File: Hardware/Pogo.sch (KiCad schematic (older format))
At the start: 3 parts

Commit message: Adjusted beginning schematics. Not much there yet
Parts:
- removed P?: CONN_6, symbol CONN_6
- added P? (x2): CONN_5X2, symbol CONN_5X2
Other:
- moved on the sheet: P?
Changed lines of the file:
@@
-EESchema Schematic File Version 2  date 5/6/2012 4:36:42 PM
+EESchema Schematic File Version 2  date 5/11/2012 5:03:51 PM
 LIBS:power
 LIBS:device
@@
 LIBS:contrib
 LIBS:valves
-EELAYER 43  0
+LIBS:Pogo-cache
+EELAYER 25  0
 EELAYER END
 $Descr A4 11700 8267
@@
 Sheet 1 1
 Title "Pogo"
-Date "6 may 2012"
+Date "12 may 2012"
 Rev "1.0"
 Comp "Projects and Stuff LLC"
@@
 $EndDescr
 $Comp
-L CONN_6 P?
-U 1 1 4FA6D806
-P 5350 3150
-F 0 "P?" V 5300 3150 60  0000 C CNN
-F 1 "CONN_6" V 5400 3150 60  0000 C CNN
-	1    5350 3150
+L CONN_5X2 P?
+U 1 1 4FADA8DA
+P 5350 3250
+F 0 "P?" H 5350 3550 60  0000 C CNN
+F 1 "CONN_5X2" V 5350 3250 50  0000 C CNN
+	1    5350 3250
+	1    0    0    -1
+$EndComp
+$Comp
+L CONN_5X2 P?
+U 1 1 4FADA8D4
+P 2650 3250
+F 0 "P?" H 2650 3550 60  0000 C CNN
+F 1 "CONN_5X2" V 2650 3250 50  0000 C CNN
+	1    2650 3250
 	1    0    0    -1
 $EndComp
@@
 L CONN_3X2 P?
 U 1 1 4FA6D7FB
-P 5350 2300
-F 0 "P?" H 5350 2550 50  0000 C CNN
-F 1 "CONN_3X2" V 5350 2350 40  0000 C CNN
-	1    5350 2300
+P 5350 2350
+F 0 "P?" H 5350 2600 50  0000 C CNN
+F 1 "CONN_3X2" V 5350 2400 40  0000 C CNN
+	1    5350 2350
 	1    0    0    -1
 $EndComp

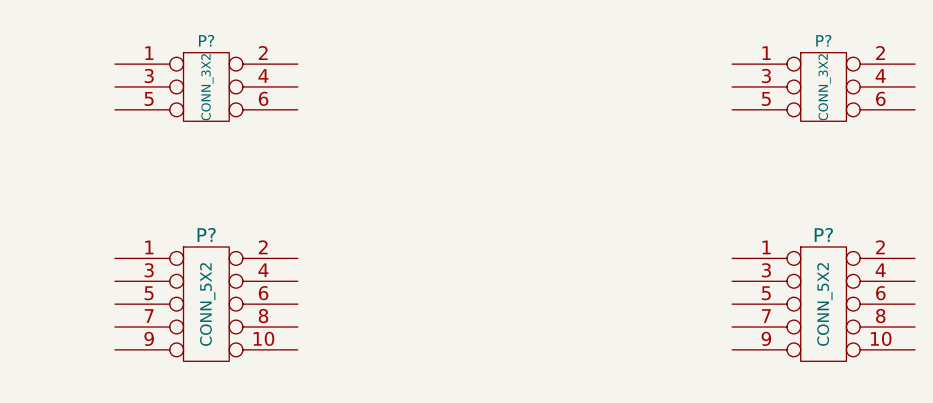
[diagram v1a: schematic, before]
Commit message: Converted BOM and updated Schematics and Board
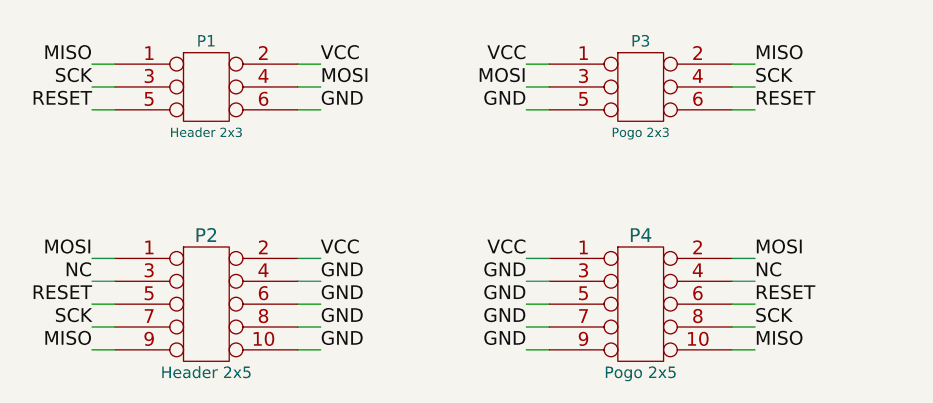
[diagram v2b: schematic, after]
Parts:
- removed P?: CONN_3X2, symbol CONN_3X2
- removed P?: CONN_5X2, symbol CONN_5X2
- added P3: Pogo 2x3, symbol CONN_3X2
- added P4: Pogo 2x5, symbol CONN_5X2
- P1: renamed from P?; value CONN_3X2 -> Header 2x3
- P2: renamed from P?; value CONN_5X2 -> Header 2x5
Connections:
- net MISO: now reaches P1.1
- net MISO: now also P2.9, P3.2, P4.10
- net VCC: now reaches P1.2
- net VCC: now also P2.2, P3.1, P4.1
- net SCK: now reaches P1.3
- net SCK: now also P2.7, P3.4, P4.8
- net MOSI: now reaches P1.4
- net MOSI: now also P2.1, P3.3, P4.2
- net RESET: now reaches P1.5
- net RESET: now also P2.5, P3.6, P4.6
- net GND: now reaches P1.6
- net GND: now also P2.10, P2.4, P2.6, P2.8, P3.5, P4.3, P4.5, P4.7, P4.9
- net NC: now reaches P2.3
- net NC: now also P4.4
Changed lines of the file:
@@
-EESchema Schematic File Version 2  date 5/11/2012 5:03:51 PM
+EESchema Schematic File Version 2  date 7/3/2012 7:28:53 PM
 LIBS:power
 LIBS:device
@@
 encoding utf-8
 Sheet 1 1
-Title "Pogo"
-Date "12 may 2012"
+Title "Pogo - A simple programmer adapter for programming AVRs using Pogo pins"
+Date "3 jul 2012"
 Rev "1.0"
 Comp "Projects and Stuff LLC"
@@
 Comment4 ""
 $EndDescr
-$Comp
-L CONN_5X2 P?
-U 1 1 4FADA8DA
-P 5350 3250
-F 0 "P?" H 5350 3550 60  0000 C CNN
-F 1 "CONN_5X2" V 5350 3250 50  0000 C CNN
-	1    5350 3250
+Text Label 5050 3450 0    60   ~ 0
+MISO
+Text Label 5050 3350 0    60   ~ 0
+SCK
+Text Label 5050 3250 0    60   ~ 0
+RESET
+Text Label 5050 3150 0    60   ~ 0
+NC
+Text Label 5050 3050 0    60   ~ 0
+MOSI
+Text Label 4050 3450 2    60   ~ 0
+GND
+Text Label 4050 3350 2    60   ~ 0
+GND
+Text Label 4050 3250 2    60   ~ 0
+GND
+Text Label 4050 3150 2    60   ~ 0
+GND
+Text Label 4050 3050 2    60   ~ 0
+VCC
+Text Label 5050 2400 0    60   ~ 0
+RESET
+Text Label 5050 2300 0    60   ~ 0
+SCK
+Text Label 5050 2200 0    60   ~ 0
+MISO
+Text Label 4050 2400 2    60   ~ 0
+GND
+Text Label 4050 2300 2    60   ~ 0
+MOSI
+Text Label 4050 2200 2    60   ~ 0
+VCC
+$Comp
+L CONN_3X2 P3
+U 1 1 4FF37E04
+P 4550 2350
+F 0 "P3" H 4550 2600 50  0000 C CNN
+F 1 "Pogo 2x3" H 4550 2200 40  0000 C CNN
+	1    4550 2350
 	1    0    0    -1
 $EndComp
 $Comp
-L CONN_5X2 P?
+L CONN_5X2 P4
+U 1 1 4FF37E03
+P 4550 3250
+F 0 "P4" H 4550 3550 60  0000 C CNN
+F 1 "Pogo 2x5" H 4550 2950 50  0000 C CNN
+	1    4550 3250
+	1    0    0    -1
+$EndComp
+Wire Wire Line
+	4950 3350 5050 3350
+Wire Wire Line
+	4950 3150 5050 3150
+Wire Wire Line
+	4150 3450 4050 3450
+Wire Wire Line
+	4150 3250 4050 3250
+Wire Wire Line
+	4150 3050 4050 3050
+Wire Wire Line
+	4950 2300 5050 2300
+Wire Wire Line
+	4150 2400 4050 2400
+Wire Wire Line
+	4150 2200 4050 2200
+Wire Wire Line
+	4150 2300 4050 2300
+Wire Wire Line
+	4950 2200 5050 2200
+Wire Wire Line
+	4950 2400 5050 2400
+Wire Wire Line
+	4150 3150 4050 3150
+Wire Wire Line
+	4150 3350 4050 3350
+Wire Wire Line
+	4950 3050 5050 3050
+Wire Wire Line
+	4950 3250 5050 3250
+Wire Wire Line
+	4950 3450 5050 3450
+Text Label 2150 3450 2    60   ~ 0
+MISO
+Text Label 2150 3350 2    60   ~ 0
+SCK
+Text Label 2150 3250 2    60   ~ 0
+RESET
+Text Label 2150 3150 2    60   ~ 0
+NC
+Text Label 2150 3050 2    60   ~ 0
+MOSI
+Text Label 3150 3450 0    60   ~ 0
+GND
+Text Label 3150 3350 0    60   ~ 0
+GND
+Text Label 3150 3250 0    60   ~ 0
+GND
+Text Label 3150 3150 0    60   ~ 0
+GND
+Text Label 3150 3050 0    60   ~ 0
+VCC
+Text Label 3150 2400 0    60   ~ 0
+GND
+Text Label 3150 2300 0    60   ~ 0
+MOSI
+Text Label 3150 2200 0    60   ~ 0
+VCC
+Text Label 2150 2400 2    60   ~ 0
+RESET
+Text Label 2150 2300 2    60   ~ 0
+SCK
+Text Label 2150 2200 2    60   ~ 0
+MISO
+Wire Wire Line
+	3050 3450 3150 3450
+Wire Wire Line
+	3050 3250 3150 3250
+Wire Wire Line
+	3050 3050 3150 3050
+Wire Wire Line
+	2250 3350 2150 3350
+Wire Wire Line
+	2250 3150 2150 3150
+Wire Wire Line
+	3050 2400 3150 2400
+Wire Wire Line
+	3050 2200 3150 2200
+Wire Wire Line
+	2250 2300 2150 2300
+Wire Wire Line
+	2250 2200 2150 2200
+Wire Wire Line
+	2250 2400 2150 2400
+Wire Wire Line
+	3050 2300 3150 2300
+Wire Wire Line
+	2250 3050 2150 3050
+Wire Wire Line
+	2250 3250 2150 3250
+Wire Wire Line
+	2250 3450 2150 3450
+Wire Wire Line
+	3050 3150 3150 3150
+Wire Wire Line
+	3050 3350 3150 3350
+$Comp
+L CONN_5X2 P2
 U 1 1 4FADA8D4
 P 2650 3250
-F 0 "P?" H 2650 3550 60  0000 C CNN
-F 1 "CONN_5X2" V 2650 3250 50  0000 C CNN
+F 0 "P2" H 2650 3550 60  0000 C CNN
+F 1 "Header 2x5" H 2650 2950 50  0000 C CNN
 	1    2650 3250
 	1    0    0    -1
 $EndComp
 $Comp
-L CONN_3X2 P?
-U 1 1 4FA6D7FB
-P 5350 2350
-F 0 "P?" H 5350 2600 50  0000 C CNN
-F 1 "CONN_3X2" V 5350 2400 40  0000 C CNN
-	1    5350 2350
-	1    0    0    -1
-$EndComp
-$Comp
-L CONN_3X2 P?
+L CONN_3X2 P1
 U 1 1 4FA6D7F4
 P 2650 2350
-F 0 "P?" H 2650 2600 50  0000 C CNN
-F 1 "CONN_3X2" V 2650 2400 40  0000 C CNN
+F 0 "P1" H 2650 2600 50  0000 C CNN
+F 1 "Header 2x3" H 2650 2200 40  0000 C CNN
 	1    2650 2350
 	1    0    0    -1
